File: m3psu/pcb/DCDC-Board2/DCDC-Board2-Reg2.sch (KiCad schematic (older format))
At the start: 38 parts

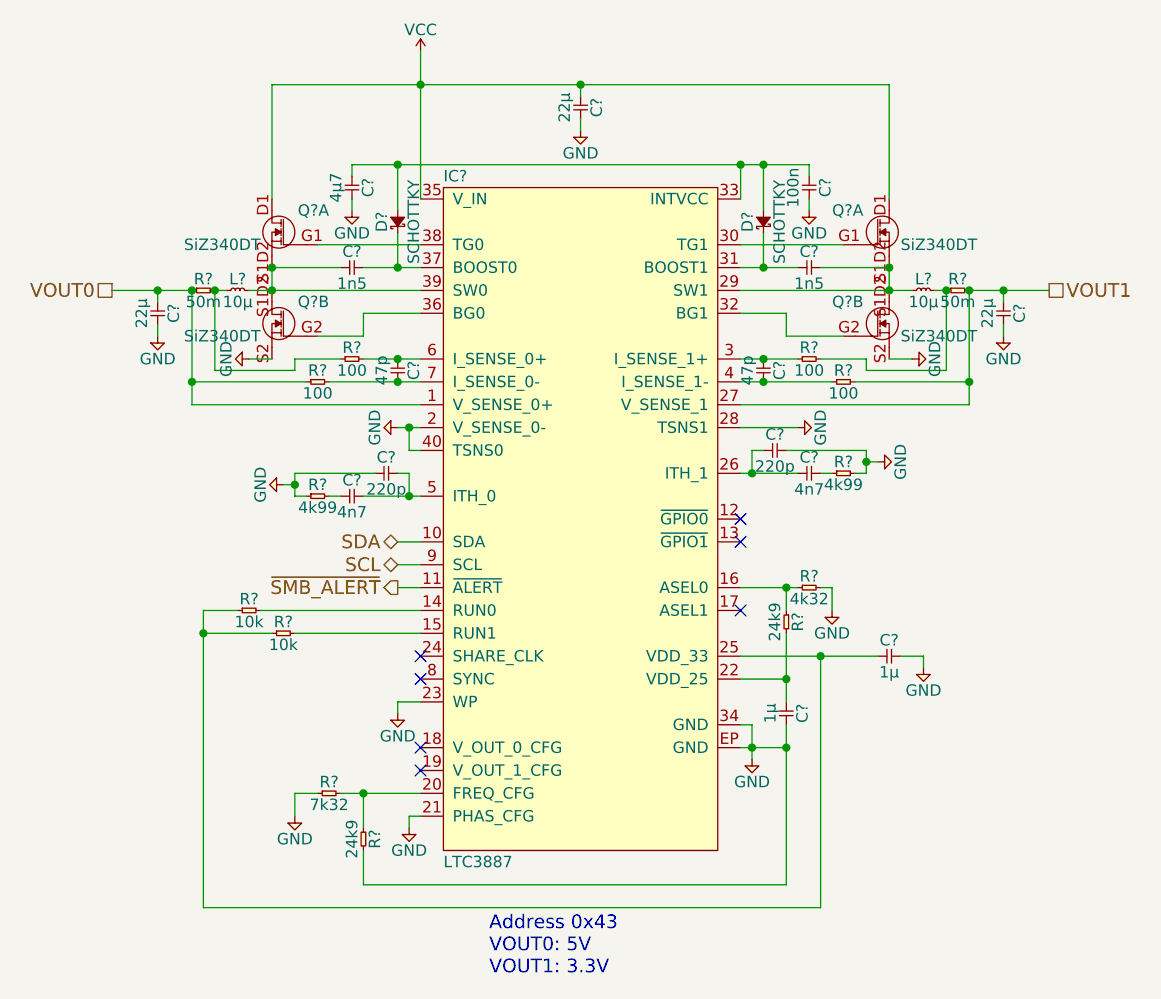
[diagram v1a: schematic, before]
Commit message: Start DC/DC routing
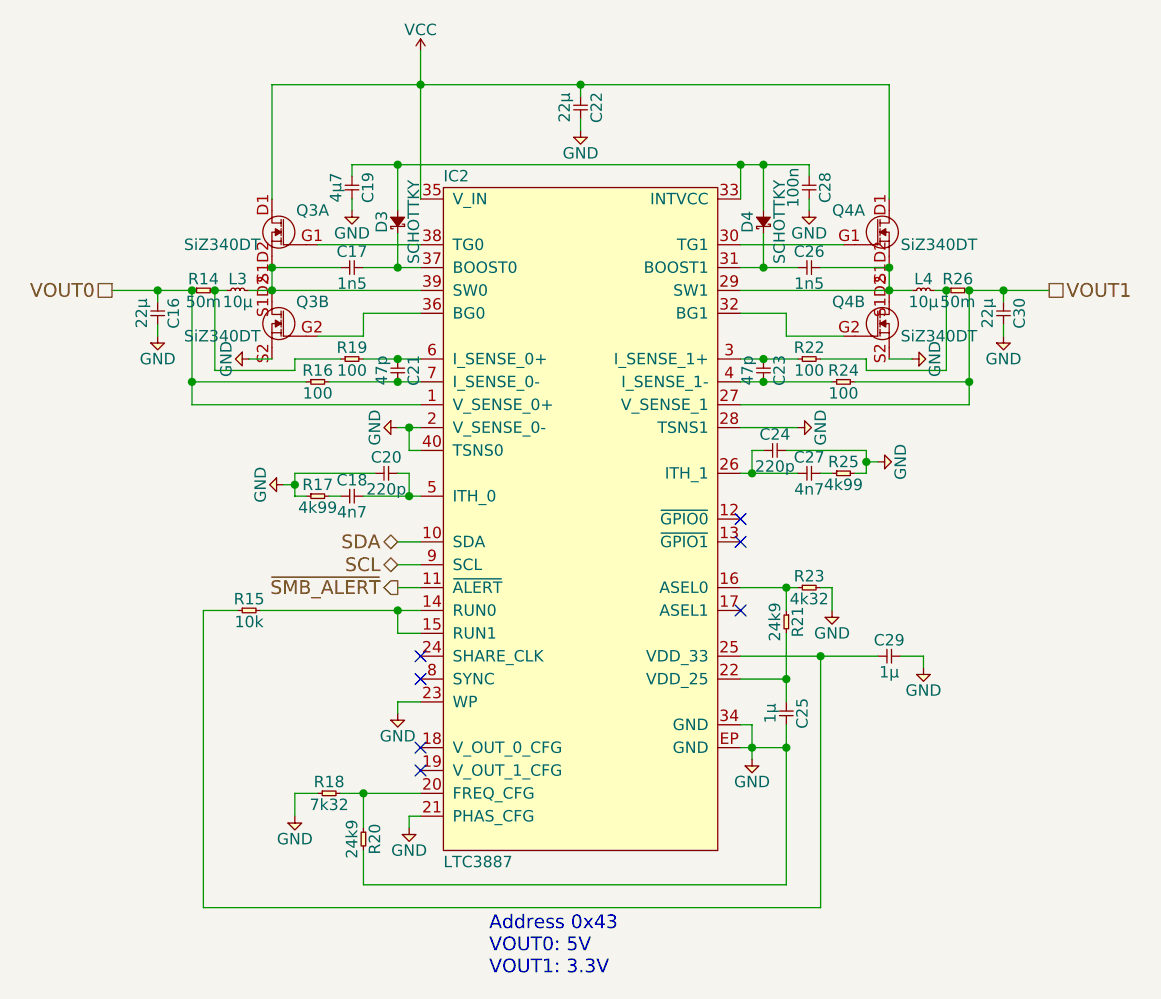
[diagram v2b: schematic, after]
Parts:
- removed R?: 10k, agg:0402, symbol R
- gave numbers to parts that had none: 35
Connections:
- net at IC2.14 (RUN0), R15.2: now also IC2.15 (RUN1)

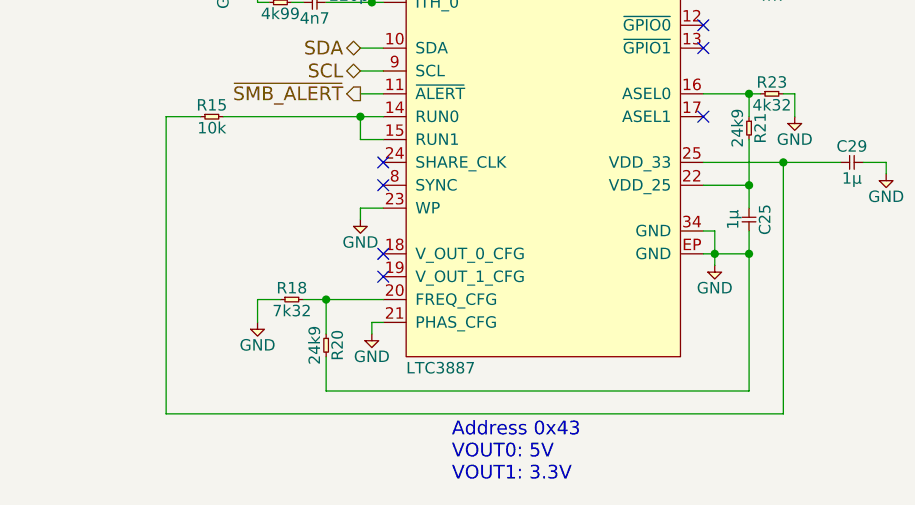
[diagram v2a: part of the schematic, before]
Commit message: Finish routing DC-DC Board 2
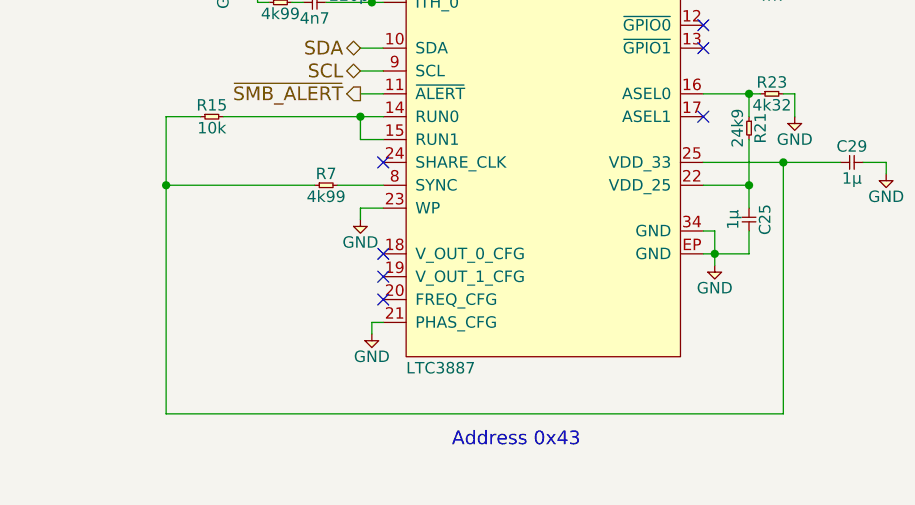
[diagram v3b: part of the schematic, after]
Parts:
- removed R18: 7k32, agg:0402, symbol R
- removed R20: 24k9, agg:0402, symbol R
- added R7: 4k99, agg:0402, symbol R
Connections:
- net at C29.1, IC2.25 (VDD_33), R15.1: now also R7.1
- net at IC2.8 (SYNC): now also R7.2
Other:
- note added: "Address 0x43"
- note removed: "Address 0x43\nVOUT0: 5V\nVOUT1: 3.3V"
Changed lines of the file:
@@
 EESchema Schematic File Version 2
 LIBS:agg-kicad
+LIBS:DCDC-Board2-cache
 EELAYER 25 0
 EELAYER END
@@
 $EndComp
 $Comp
-L VCC #PWR041
+L VCC #PWR040
 U 1 1 56D586F4
 P 5150 1850
-F 0 "#PWR041" H 5150 1960 50  0001 L CNN
+F 0 "#PWR040" H 5150 1960 50  0001 L CNN
 F 1 "VCC" H 5150 1940 50  0000 C CNN
 F 2 "" H 5150 1850 60  0000 C CNN
@@
 $EndComp
 $Comp
-L GND #PWR042
+L GND #PWR041
 U 1 1 56D58702
 P 4850 2550
-F 0 "#PWR042" H 4720 2590 50  0001 L CNN
+F 0 "#PWR041" H 4720 2590 50  0001 L CNN
 F 1 "GND" H 4850 2450 50  0000 C CNN
 F 2 "" H 4850 2550 60  0000 C CNN
@@
 $EndComp
 $Comp
-L GND #PWR043
+L GND #PWR042
 U 1 1 56D58710
 P 5850 2200
-F 0 "#PWR043" H 5720 2240 50  0001 L CNN
+F 0 "#PWR042" H 5720 2240 50  0001 L CNN
 F 1 "GND" H 5850 2100 50  0000 C CNN
 F 2 "" H 5850 2200 60  0000 C CNN
@@
 $EndComp
 $Comp
-L GND #PWR044
+L GND #PWR043
 U 1 1 56D5873E
 P 7700 3100
-F 0 "#PWR044" H 7570 3140 50  0001 L CNN
+F 0 "#PWR043" H 7570 3140 50  0001 L CNN
 F 1 "GND" H 7700 3000 50  0000 C CNN
 F 2 "" H 7700 3100 60  0000 C CNN
@@
 $EndComp
 $Comp
-L GND #PWR045
+L GND #PWR044
 U 1 1 56D5874C
 P 4000 3100
-F 0 "#PWR045" H 3870 3140 50  0001 L CNN
+F 0 "#PWR044" H 3870 3140 50  0001 L CNN
 F 1 "GND" H 4000 3000 50  0000 C CNN
 F 2 "" H 4000 3100 60  0000 C CNN
@@
 $EndComp
 $Comp
-L GND #PWR046
+L GND #PWR045
 U 1 1 56D58772
 P 6600 4950
-F 0 "#PWR046" H 6470 4990 50  0001 L CNN
+F 0 "#PWR045" H 6470 4990 50  0001 L CNN
 F 1 "GND" H 6600 4850 50  0000 C CNN
 F 2 "" H 6600 4950 60  0000 C CNN
@@
 $EndComp
 $Comp
-L GND #PWR047
+L GND #PWR046
 U 1 1 56D58788
 P 5050 3500
-F 0 "#PWR047" H 4920 3540 50  0001 L CNN
+F 0 "#PWR046" H 4920 3540 50  0001 L CNN
 F 1 "GND" H 5050 3400 50  0000 C CNN
 F 2 "" H 5050 3500 60  0000 C CNN
@@
 $EndComp
 $Comp
-L GND #PWR048
+L GND #PWR047
 U 1 1 56D5878E
 P 4400 3200
-F 0 "#PWR048" H 4270 3240 50  0001 L CNN
+F 0 "#PWR047" H 4270 3240 50  0001 L CNN
 F 1 "GND" H 4400 3100 50  0000 C CNN
 F 2 "" H 4400 3200 60  0000 C CNN
@@
 $EndComp
 $Comp
-L GND #PWR049
+L GND #PWR048
 U 1 1 56D58794
 P 7300 3200
-F 0 "#PWR049" H 7170 3240 50  0001 L CNN
+F 0 "#PWR048" H 7170 3240 50  0001 L CNN
 F 1 "GND" H 7300 3100 50  0000 C CNN
 F 2 "" H 7300 3200 60  0000 C CNN
@@
 $EndComp
 $Comp
-L GND #PWR050
+L GND #PWR049
 U 1 1 56D587B2
 P 6850 2550
-F 0 "#PWR050" H 6720 2590 50  0001 L CNN
+F 0 "#PWR049" H 6720 2590 50  0001 L CNN
 F 1 "GND" H 6850 2450 50  0000 C CNN
 F 2 "" H 6850 2550 60  0000 C CNN
@@
 $EndComp
 $Comp
-L GND #PWR051
+L GND #PWR050
 U 1 1 56D587B8
 P 7350 4550
-F 0 "#PWR051" H 7220 4590 50  0001 L CNN
+F 0 "#PWR050" H 7220 4590 50  0001 L CNN
 F 1 "GND" H 7350 4450 50  0000 C CNN
 F 2 "" H 7350 4550 60  0000 C CNN
@@
 SCL
 $Comp
-L GND #PWR052
+L GND #PWR051
 U 1 1 56D587F8
 P 5050 4750
-F 0 "#PWR052" H 4920 4790 50  0001 L CNN
+F 0 "#PWR051" H 4920 4790 50  0001 L CNN
 F 1 "GND" H 5050 4650 50  0000 C CNN
 F 2 "" H 5050 4750 60  0000 C CNN
@@
 $EndComp
 NoConn ~ 5150 4500
-NoConn ~ 5150 4600
 NoConn ~ 6550 4300
 $Comp
@@
 $EndComp
 $Comp
-L GND #PWR053
+L GND #PWR052
 U 1 1 56D58809
 P 6950 4300
-F 0 "#PWR053" H 6820 4340 50  0001 L CNN
+F 0 "#PWR052" H 6820 4340 50  0001 L CNN
 F 1 "GND" H 6950 4200 50  0000 C CNN
 F 2 "" H 6950 4300 60  0000 C CNN
@@
 $EndComp
 $Comp
-L GND #PWR054
+L GND #PWR053
 U 1 1 56D5881F
 P 7150 3650
-F 0 "#PWR054" H 7020 3690 50  0001 L CNN
+F 0 "#PWR053" H 7020 3690 50  0001 L CNN
 F 1 "GND" H 7150 3550 50  0000 C CNN
 F 2 "" H 7150 3650 60  0000 C CNN
@@
 $EndComp
 $Comp
-L GND #PWR055
+L GND #PWR054
 U 1 1 56D5883D
 P 4550 3750
-F 0 "#PWR055" H 4420 3790 50  0001 L CNN
+F 0 "#PWR054" H 4420 3790 50  0001 L CNN
 F 1 "GND" H 4550 3650 50  0000 C CNN
 F 2 "" H 4550 3750 60  0000 C CNN
@@
 $EndComp
 $Comp
-L GND #PWR056
+L GND #PWR055
 U 1 1 56D58843
 P 5100 5250
-F 0 "#PWR056" H 4970 5290 50  0001 L CNN
+F 0 "#PWR055" H 4970 5290 50  0001 L CNN
 F 1 "GND" H 5100 5150 50  0000 C CNN
 F 2 "" H 5100 5250 60  0000 C CNN
@@
 Wire Wire Line
 	5100 5200 5150 5200
-Connection ~ 6750 4900
 Wire Wire Line
 	7250 4500 7350 4500
@@
 Wire Wire Line
 	5050 3500 5150 3500
-Wire Wire Line
-	6750 4800 6750 5500
 Wire Wire Line
 	6550 4500 7150 4500
@@
 Connection ~ 5100 3500
 $Comp
-L GND #PWR057
+L GND #PWR056
 U 1 1 56D588E8
 P 6800 3500
-F 0 "#PWR057" H 6670 3540 50  0001 L CNN
+F 0 "#PWR056" H 6670 3540 50  0001 L CNN
 F 1 "GND" H 6800 3400 50  0000 C CNN
 F 2 "" H 6800 3500 60  0000 C CNN
@@
 Text HLabel 5050 4200 0    60   Output ~ 0
 ~SMB_ALERT
-Text Notes 5450 5900 0    60   ~ 0
-Address 0x43\nVOUT0: 5V\nVOUT1: 3.3V
+Text Notes 5450 5750 0    60   ~ 0
+Address 0x43
 Wire Wire Line
 	5050 4700 5150 4700
-$Comp
-L R R20
-U 1 1 56DDD708
-P 4900 5250
-F 0 "R20" H 4950 5300 50  0000 C CNN
-F 1 "24k9" H 4950 5200 50  0000 C CNN
-F 2 "agg:0402" H 4900 5250 50  0001 C CNN
-F 3 "" H 4900 5250 50  0001 C CNN
-F 4 "1803690" H 4900 5250 60  0001 C CNN "Farnell"
-	1    4900 5250
-	0    1    1    0
-$EndComp
-$Comp
-L GND #PWR058
-U 1 1 56DDD70F
-P 4600 5200
-F 0 "#PWR058" H 4470 5240 50  0001 L CNN
-F 1 "GND" H 4600 5100 50  0000 C CNN
-F 2 "" H 4600 5200 60  0000 C CNN
-F 3 "" H 4600 5200 60  0000 C CNN
-	1    4600 5200
-	1    0    0    -1
-$EndComp
-Connection ~ 4900 5100
-Wire Wire Line
-	4800 5100 5150 5100
-Wire Wire Line
-	4900 5100 4900 5250
-Wire Wire Line
-	4900 5350 4900 5500
-$Comp
-L R R18
-U 1 1 56DDD71A
-P 4700 5100
-F 0 "R18" H 4750 5150 50  0000 C CNN
-F 1 "7k32" H 4750 5050 50  0000 C CNN
-F 2 "agg:0402" H 4700 5100 50  0001 C CNN
-F 3 "" H 4700 5100 50  0001 C CNN
-F 4 "2073231" H 4700 5100 60  0001 C CNN "Farnell"
-	1    4700 5100
-	1    0    0    -1
-$EndComp
-Wire Wire Line
-	4700 5100 4600 5100
-Wire Wire Line
-	4600 5100 4600 5200
-Wire Wire Line
-	4900 5500 6750 5500
 Wire Wire Line
 	4200 5600 6900 5600
@@
 	5050 4400 5050 4300
 Connection ~ 5050 4300
+Wire Wire Line
+	6750 4900 6750 4800
+NoConn ~ 5150 5100
+$Comp
+L R R7
+U 1 1 5717E02F
+P 4850 4600
+F 0 "R7" H 4900 4650 50  0000 C CNN
+F 1 "4k99" H 4900 4550 50  0000 C CNN
+F 2 "agg:0402" H 4850 4600 50  0001 C CNN
+F 3 "" H 4850 4600 50  0001 C CNN
+F 4 "1469715" H 4850 4600 60  0001 C CNN "Farnell"
+	1    4850 4600
+	1    0    0    -1
+$EndComp
+Wire Wire Line
+	5150 4600 4950 4600
+Wire Wire Line
+	4850 4600 4200 4600
+Connection ~ 4200 4600
 $EndSCHEMATC

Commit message: Fixed GPIO 1&2 pull to VDD33 with 10k. Fixed V_IN 100n decoupling cap. Fixed BOOST caps to 100n.
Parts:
- added C32: 100n, agg:0402, symbol C
- added R20: 10k, agg:0402, symbol R
- C17, C26: value 1n5 -> 100n; Farnell 2210833 -> 2496811
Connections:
- net GND: now also C32.2
- net VCC: now also C32.1
- net at IC2.12 (~GPIO0): now also IC2.13 (~GPIO1), R20.1
- net at C29.1, IC2.25 (VDD_33), R15.1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: now also R20.2
- no-connect marks 7 -> 5
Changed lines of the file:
@@
 P 6800 2800
 F 0 "C26" H 6850 2870 50  0000 C CNN
-F 1 "1n5" H 6850 2730 50  0000 C CNN
+F 1 "100n" H 6850 2730 50  0000 C CNN
 F 2 "agg:0402" H 6800 2800 50  0001 C CNN
 F 3 "" H 6800 2800 50  0001 C CNN
-F 4 "2210833" H 6800 2800 60  0001 C CNN "Farnell"
+F 4 "2496811" H 6800 2800 60  0001 C CNN "Farnell"
 	1    6800 2800
 	1    0    0    -1
@@
 P 4800 2800
 F 0 "C17" H 4850 2870 50  0000 C CNN
-F 1 "1n5" H 4850 2730 50  0000 C CNN
+F 1 "100n" H 4850 2730 50  0000 C CNN
 F 2 "agg:0402" H 4800 2800 50  0001 C CNN
 F 3 "" H 4800 2800 50  0001 C CNN
-F 4 "2210833" H 4800 2800 60  0001 C CNN "Farnell"
+F 4 "2496811" H 4800 2800 60  0001 C CNN "Farnell"
 	1    4800 2800
 	1    0    0    -1
@@
 $EndComp
 $Comp
-L VCC #PWR040
+L VCC #PWR041
 U 1 1 56D586F4
 P 5150 1850
-F 0 "#PWR040" H 5150 1960 50  0001 L CNN
+F 0 "#PWR041" H 5150 1960 50  0001 L CNN
 F 1 "VCC" H 5150 1940 50  0000 C CNN
 F 2 "" H 5150 1850 60  0000 C CNN
@@
 $EndComp
 $Comp
-L GND #PWR041
+L GND #PWR042
 U 1 1 56D58702
 P 4850 2550
-F 0 "#PWR041" H 4720 2590 50  0001 L CNN
+F 0 "#PWR042" H 4720 2590 50  0001 L CNN
 F 1 "GND" H 4850 2450 50  0000 C CNN
 F 2 "" H 4850 2550 60  0000 C CNN
@@
 $EndComp
 $Comp
-L GND #PWR042
+L GND #PWR043
 U 1 1 56D58710
 P 5850 2200
-F 0 "#PWR042" H 5720 2240 50  0001 L CNN
+F 0 "#PWR043" H 5720 2240 50  0001 L CNN
 F 1 "GND" H 5850 2100 50  0000 C CNN
 F 2 "" H 5850 2200 60  0000 C CNN
@@
 $EndComp
 $Comp
-L GND #PWR043
+L GND #PWR044
 U 1 1 56D5873E
 P 7700 3100
-F 0 "#PWR043" H 7570 3140 50  0001 L CNN
+F 0 "#PWR044" H 7570 3140 50  0001 L CNN
 F 1 "GND" H 7700 3000 50  0000 C CNN
 F 2 "" H 7700 3100 60  0000 C CNN
@@
 $EndComp
 $Comp
-L GND #PWR044
+L GND #PWR045
 U 1 1 56D5874C
 P 4000 3100
-F 0 "#PWR044" H 3870 3140 50  0001 L CNN
+F 0 "#PWR045" H 3870 3140 50  0001 L CNN
 F 1 "GND" H 4000 3000 50  0000 C CNN
 F 2 "" H 4000 3100 60  0000 C CNN
@@
 $EndComp
 $Comp
-L GND #PWR045
+L GND #PWR046
 U 1 1 56D58772
 P 6600 4950
-F 0 "#PWR045" H 6470 4990 50  0001 L CNN
+F 0 "#PWR046" H 6470 4990 50  0001 L CNN
 F 1 "GND" H 6600 4850 50  0000 C CNN
 F 2 "" H 6600 4950 60  0000 C CNN
@@
 $EndComp
 $Comp
-L GND #PWR046
+L GND #PWR047
 U 1 1 56D58788
 P 5050 3500
-F 0 "#PWR046" H 4920 3540 50  0001 L CNN
+F 0 "#PWR047" H 4920 3540 50  0001 L CNN
 F 1 "GND" H 5050 3400 50  0000 C CNN
 F 2 "" H 5050 3500 60  0000 C CNN
@@
 $EndComp
 $Comp
-L GND #PWR047
+L GND #PWR048
 U 1 1 56D5878E
 P 4400 3200
-F 0 "#PWR047" H 4270 3240 50  0001 L CNN
+F 0 "#PWR048" H 4270 3240 50  0001 L CNN
 F 1 "GND" H 4400 3100 50  0000 C CNN
 F 2 "" H 4400 3200 60  0000 C CNN
@@
 $EndComp
 $Comp
-L GND #PWR048
+L GND #PWR049
 U 1 1 56D58794
 P 7300 3200
-F 0 "#PWR048" H 7170 3240 50  0001 L CNN
+F 0 "#PWR049" H 7170 3240 50  0001 L CNN
 F 1 "GND" H 7300 3100 50  0000 C CNN
 F 2 "" H 7300 3200 60  0000 C CNN
@@
 $EndComp
 $Comp
-L GND #PWR049
+L GND #PWR050
 U 1 1 56D587B2
 P 6850 2550
-F 0 "#PWR049" H 6720 2590 50  0001 L CNN
+F 0 "#PWR050" H 6720 2590 50  0001 L CNN
 F 1 "GND" H 6850 2450 50  0000 C CNN
 F 2 "" H 6850 2550 60  0000 C CNN
@@
 $EndComp
 $Comp
-L GND #PWR050
+L GND #PWR051
 U 1 1 56D587B8
 P 7350 4550
-F 0 "#PWR050" H 7220 4590 50  0001 L CNN
+F 0 "#PWR051" H 7220 4590 50  0001 L CNN
 F 1 "GND" H 7350 4450 50  0000 C CNN
 F 2 "" H 7350 4550 60  0000 C CNN
@@
 SCL
 $Comp
-L GND #PWR051
+L GND #PWR052
 U 1 1 56D587F8
 P 5050 4750
-F 0 "#PWR051" H 4920 4790 50  0001 L CNN
+F 0 "#PWR052" H 4920 4790 50  0001 L CNN
 F 1 "GND" H 5050 4650 50  0000 C CNN
 F 2 "" H 5050 4750 60  0000 C CNN
@@
 $EndComp
 $Comp
-L GND #PWR052
+L GND #PWR053
 U 1 1 56D58809
 P 6950 4300
-F 0 "#PWR052" H 6820 4340 50  0001 L CNN
+F 0 "#PWR053" H 6820 4340 50  0001 L CNN
 F 1 "GND" H 6950 4200 50  0000 C CNN
 F 2 "" H 6950 4300 60  0000 C CNN
@@
 $EndComp
 $Comp
-L GND #PWR053
+L GND #PWR054
 U 1 1 56D5881F
 P 7150 3650
-F 0 "#PWR053" H 7020 3690 50  0001 L CNN
+F 0 "#PWR054" H 7020 3690 50  0001 L CNN
 F 1 "GND" H 7150 3550 50  0000 C CNN
 F 2 "" H 7150 3650 60  0000 C CNN
@@
 $EndComp
 $Comp
-L GND #PWR054
+L GND #PWR055
 U 1 1 56D5883D
 P 4550 3750
-F 0 "#PWR054" H 4420 3790 50  0001 L CNN
+F 0 "#PWR055" H 4420 3790 50  0001 L CNN
 F 1 "GND" H 4550 3650 50  0000 C CNN
 F 2 "" H 4550 3750 60  0000 C CNN
@@
 $EndComp
 $Comp
-L GND #PWR055
+L GND #PWR056
 U 1 1 56D58843
 P 5100 5250
-F 0 "#PWR055" H 4970 5290 50  0001 L CNN
+F 0 "#PWR056" H 4970 5290 50  0001 L CNN
 F 1 "GND" H 5100 5150 50  0000 C CNN
 F 2 "" H 5100 5250 60  0000 C CNN
@@
 Connection ~ 5100 3500
 $Comp
-L GND #PWR056
+L GND #PWR057
 U 1 1 56D588E8
 P 6800 3500
-F 0 "#PWR056" H 6670 3540 50  0001 L CNN
+F 0 "#PWR057" H 6670 3540 50  0001 L CNN
 F 1 "GND" H 6800 3400 50  0000 C CNN
 F 2 "" H 6800 3500 60  0000 C CNN
@@
 Wire Wire Line
 	6550 3500 6800 3500
-NoConn ~ 6550 3900
-NoConn ~ 6550 4000
 $Comp
 L C C24
@@
 	4850 4600 4200 4600
 Connection ~ 4200 4600
+Wire Wire Line
+	6550 3900 6600 3900
+Wire Wire Line
+	6600 3900 6600 4000
+Wire Wire Line
+	6600 4000 6550 4000
+$Comp
+L R R20
+U 1 1 574746C5
+P 7050 4050
+F 0 "R20" H 7100 4100 50  0000 C CNN
+F 1 "10k" H 7100 4000 50  0000 C CNN
+F 2 "agg:0402" H 7050 4050 50  0001 C CNN
+F 3 "" H 7050 4050 50  0001 C CNN
+F 4 "2447096" H 7050 4050 60  0001 C CNN "Farnell"
+	1    7050 4050
+	0    1    1    0
+$EndComp
+Wire Wire Line
+	7050 4050 7050 3950
+Wire Wire Line
+	7050 3950 6600 3950
+Connection ~ 6600 3950
+Wire Wire Line
+	7050 4150 7050 4500
+Connection ~ 7050 4500
+$Comp
+L C C32
+U 1 1 57476DF7
+P 5200 2150
+F 0 "C32" H 5250 2220 50  0000 C CNN
+F 1 "100n" H 5250 2080 50  0000 C CNN
+F 2 "agg:0402" H 5200 2150 50  0001 C CNN
+F 3 "" H 5200 2150 50  0001 C CNN
+F 4 "2496811" H 5200 2150 60  0001 C CNN "Farnell"
+	1    5200 2150
+	1    0    0    -1
+$EndComp
+$Comp
+L GND #PWR058
+U 1 1 57476EC2
+P 5400 2200
+F 0 "#PWR058" H 5270 2240 50  0001 L CNN
+F 1 "GND" H 5400 2100 50  0000 C CNN
+F 2 "" H 5400 2200 60  0000 C CNN
+F 3 "" H 5400 2200 60  0000 C CNN
+	1    5400 2200
+	1    0    0    -1
+$EndComp
+Wire Wire Line
+	5300 2150 5400 2150
+Wire Wire Line
+	5400 2150 5400 2200
+Wire Wire Line
+	5200 2150 5150 2150
+Connection ~ 5150 2150
 $EndSCHEMATC
